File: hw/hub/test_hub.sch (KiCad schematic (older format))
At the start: 104 parts, among them J1 ARM-SWD, P1 USB_OTG, P2 5V_SEL, P3 5V_EXT, P4 USB1, P5 USB2, P6 USB3, P7 UART, SW1 RST, SW2 BOOT, U1 USB2514B, U2 MIC550X, U3 stm32f072x, U4 AP2171, U5 AP2171, U6 AP2171, U7 LT6106, U8 LT6106, U9 LT6106, Y1 24MHz

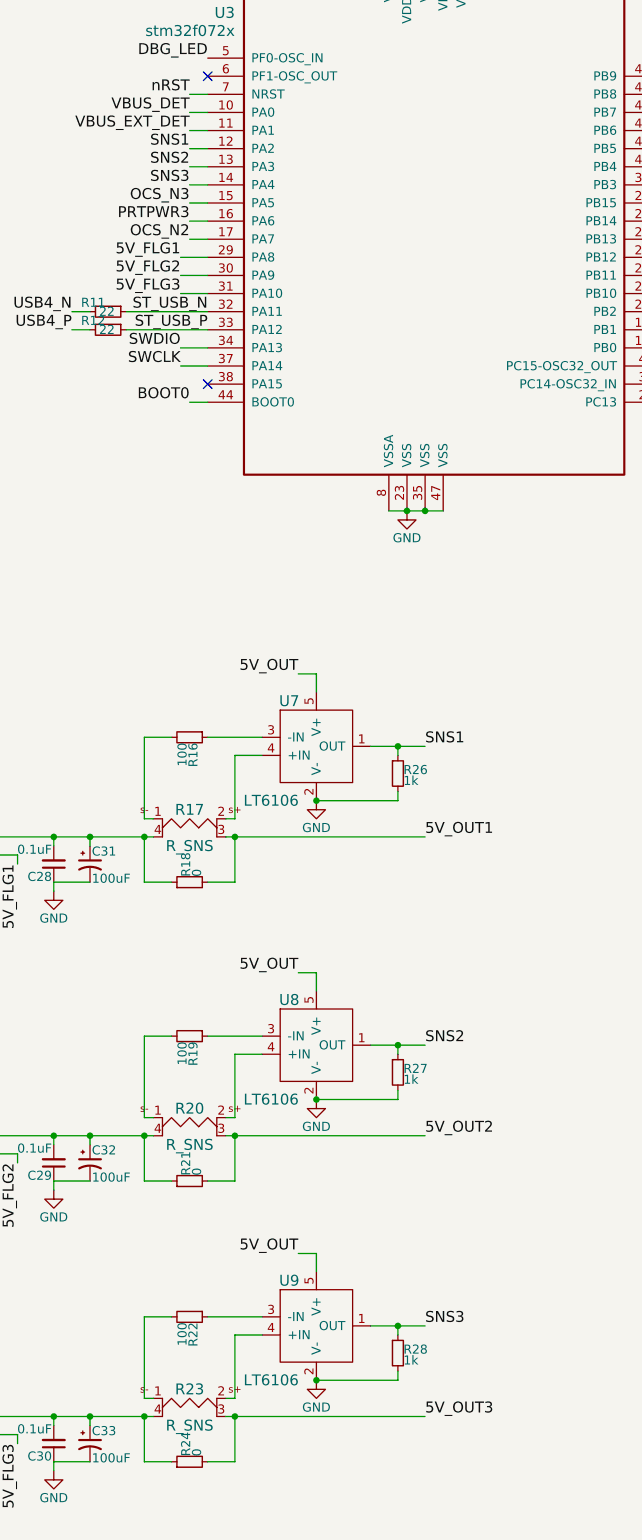
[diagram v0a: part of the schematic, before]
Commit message: Begin removing sense resistors from hub
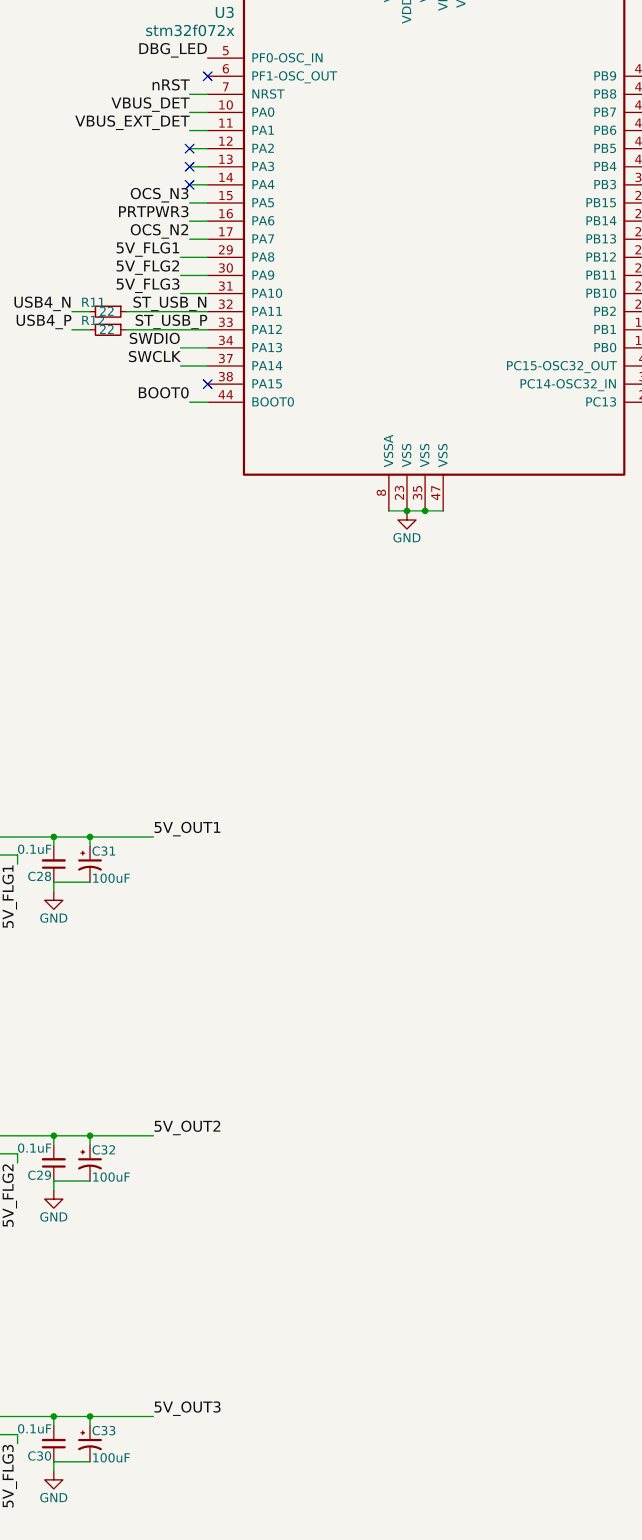
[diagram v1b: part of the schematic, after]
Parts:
- removed R16, R19, R22: 100, Resistors_SMD:R_0603, symbol R_Small
- removed R17, R20, R23: R_SNS, footprints:LVK12, symbol R_SNS
- removed R18, R21, R24: 0, Resistors_SMD:R_0603, symbol R_Small
- removed R26, R27, R28: 1k, Resistors_SMD:R_0603, symbol R_Small
- removed U7, U8, U9: LT6106, footprints:TSOT-23-5, symbol LT6106-RESCUE-test_hub
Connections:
- net 5V_OUT1: now also C28.2, C31.1, U4.1 (OUT)
- net 5V_OUT2: now also C29.2, C32.1, U5.1 (OUT)
- net 5V_OUT3: now also C30.2, C33.1, U6.1 (OUT)
- net SNS1: no longer names the net of U3.12 (PA2)
- net SNS2: no longer names the net of U3.13 (PA3)
- net SNS3: no longer names the net of U3.14 (PA4)
- no-connect marks 13 -> 16

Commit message: Update test_hub
No more rescued components
Ripped up all traces
Starting layout again
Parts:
- removed D1: 3V, LEDs:LED_0603, symbol LED-RESCUE-test_hub
- removed D2: DBG, LEDs:LED_0603, symbol LED-RESCUE-test_hub
- removed D3: 5V_EN3, LEDs:LED_0603, symbol LED-RESCUE-test_hub
- removed D4: 5V_EN2, LEDs:LED_0603, symbol LED-RESCUE-test_hub
- removed D5: 5V_EN1, LEDs:LED_0603, symbol LED-RESCUE-test_hub
- removed D6: LED2, LEDs:LED_0603, symbol LED-RESCUE-test_hub
- removed D7: LED1, LEDs:LED_0603, symbol LED-RESCUE-test_hub
- removed D8: LED0, LEDs:LED_0603, symbol LED-RESCUE-test_hub
- removed P1: USB_OTG, footprints:10118193-0001LF, symbol USB_OTG-RESCUE-test_hub
- removed P4: USB1, footprints:292303-1, symbol USB_A-RESCUE-test_hub
- removed P5: USB2, footprints:292303-1, symbol USB_A-RESCUE-test_hub
- removed P6: USB3, footprints:292303-1, symbol USB_A-RESCUE-test_hub
- added C35: 0.1uF, Capacitors_SMD:C_0603, symbol C_Small
- added D1: 3V, LEDs:LED_0805, symbol LED
- added D2: DBG, LEDs:LED_0805, symbol LED
- added D3: 5V_EN3, LEDs:LED_0805, symbol LED
- added D4: 5V_EN2, LEDs:LED_0805, symbol LED
- added D5: 5V_EN1, LEDs:LED_0805, symbol LED
- added D6: LED3, LEDs:LED_0805, symbol LED
- added D7: LED2, LEDs:LED_0805, symbol LED
- added D8: LED1, LEDs:LED_0805, symbol LED
- added FB10, FB7, FB8, FB9: Ferrite_Bead, Resistors_SMD:R_0603, symbol Ferrite_Bead-RESCUE-test_hub
- added J2, J3: USB_OTG, footprints:USB_MICRO_B, symbol USB_OTG
- added J4, J5, J6: USB_A, footprints:292303-1, symbol USB_A
- added R16: 330, Resistors_SMD:R_0603, symbol R_Small
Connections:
- net LED0 is gone; now on net LED1: R36.2, U3.2 (PC13)
- net +5V: now also FB3.2, FB5.1
- net 5V_OUT2: now also FB8.1; no longer FB4.1
- net 5V_OUT3: now also FB10.1; no longer FB6.1
- net GND: now also FB4.2, FB6.1, C35.1, D1.1 (K), D2.1 (K), D3.1 (K), D4.1 (K), D5.1 (K), D6.1 (K), D7.1 (K), D8.1 (K), FB7.1, FB9.1, R16.2; no longer FB3.1, FB5.1
- net GNDPWR: now also C35.2, J2.6 (Shield), J3.6 (Shield), J4.5 (Shield), J5.5 (Shield), J6.5 (Shield), R16.1
- net LED1: no longer R35.2, U3.3 (PC14-OSC32_IN)
- net LED2: now also R35.2, U3.3 (PC14-OSC32_IN); no longer R34.2, U3.4 (PC15-OSC32_OUT)
- net USB1_N: now also J4.2 (D-)
- net USB1_P: now also J4.3 (D+)
- net USB2_N: now also J5.2 (D-)
- net USB2_P: now also J5.3 (D+)
- net USB3_N: now also J6.2 (D-)
- net USB3_P: now also J6.3 (D+)
- net USB_UP_N: now also J2.2 (D-)
- net USB_UP_P: now also J2.3 (D+)
- net at FB6.2: now also J3.5 (GND)
- net at FB5.2: now also J3.1 (VBUS)
- net at R30.1: now also D2.2 (A)
- net at R31.1: now also D3.2 (A)
- net at R32.1: now also D4.2 (A)
- net at R33.1: now also D5.2 (A)
- net at R34.1: now also D6.2 (A)
- net at R35.1: now also D7.2 (A)
- net at R36.1: now also D8.2 (A)
- net at FB1.2: now also J4.4 (GND)
- net at FB2.2: now also J4.1 (VBUS)
- net at R29.1: now also D1.2 (A)
- new net: FB3.1, J2.1 (VBUS)
- new net: FB4.1, J2.5 (GND)
- new net: FB7.2, J5.4 (GND)
- new net: FB8.2, J5.1 (VBUS)
- new net: FB9.2, J6.4 (GND)
- new net: FB10.2, J6.1 (VBUS)
- new net LED3: R34.2, U3.4 (PC15-OSC32_OUT)
- no-connect marks 16 -> 19
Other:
- moved on the sheet: C14, C15, FB1, FB2, P2, P3, R10, R7, R8, R9

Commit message: More test_hub work
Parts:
- added C36, C37: 1uF, Capacitors_SMD:C_0603, symbol C_Small
- FB1, FB10, FB2, FB3, FB4, FB5, FB6, FB7, FB8, FB9: MPN BLM18EG221SN1D -> CIS10P221NC
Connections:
- net GND: now also C36.1, C37.1
- net at C3.2, U1.14 (CRFILT): now also C37.2
- net at C4.2, U1.34 (PLLFILT): now also C36.2
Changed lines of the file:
@@
 F 2 "Resistors_SMD:R_0603" H 14450 3250 60  0001 C CNN
 F 3 "" H 14450 3250 60  0000 C CNN
-F 4 "BLM18EG221SN1D" H 14450 3200 60  0001 C CNN "MPN"
+F 4 "CIS10P221NC" H 14450 3200 60  0001 C CNN "MPN"
 	1    14450 3200
 	1    0    0    -1
@@
 F 2 "Resistors_SMD:R_0603" H 14450 3900 60  0001 C CNN
 F 3 "" H 14450 3900 60  0000 C CNN
-F 4 "BLM18EG221SN1D" H 14450 3850 60  0001 C CNN "MPN"
+F 4 "CIS10P221NC" H 14450 3850 60  0001 C CNN "MPN"
 	1    14450 3850
 	1    0    0    -1
@@
 F 2 "Resistors_SMD:R_0603" H 2450 7200 60  0001 C CNN
 F 3 "" H 2450 7200 60  0000 C CNN
-F 4 "BLM18EG221SN1D" H 2450 7150 60  0001 C CNN "MPN"
+F 4 "CIS10P221NC" H 2450 7150 60  0001 C CNN "MPN"
 	1    2450 7150
 	1    0    0    -1
@@
 F 2 "Resistors_SMD:R_0603" H 2450 7850 60  0001 C CNN
 F 3 "" H 2450 7850 60  0000 C CNN
-F 4 "BLM18EG221SN1D" H 2450 7800 60  0001 C CNN "MPN"
+F 4 "CIS10P221NC" H 2450 7800 60  0001 C CNN "MPN"
 	1    2450 7800
 	1    0    0    -1
@@
 	2050 4100 2050 4150
 Wire Wire Line
-	2850 4100 2050 4100
+	1800 4100 2850 4100
 Connection ~ 2450 5800
 Wire Wire Line
 	2450 5800 2450 5850
 Wire Wire Line
-	2700 5800 2450 5800
+	2200 5800 2700 5800
 Wire Wire Line
 	2850 5600 2700 5600
@@
 	2450 5500 2450 5600
 Wire Wire Line
-	2450 5500 2850 5500
+	2200 5500 2850 5500
 Wire Wire Line
 	2850 4800 2650 4800
@@
 F 2 "Resistors_SMD:R_0603" H 2450 8600 60  0001 C CNN
 F 3 "" H 2450 8600 60  0000 C CNN
-F 4 "BLM18EG221SN1D" H 2450 8550 60  0001 C CNN "MPN"
+F 4 "CIS10P221NC" H 2450 8550 60  0001 C CNN "MPN"
 	1    2450 8550
 	-1   0    0    1
@@
 F 2 "Resistors_SMD:R_0603" H 2450 9250 60  0001 C CNN
 F 3 "" H 2450 9250 60  0000 C CNN
-F 4 "BLM18EG221SN1D" H 2450 9200 60  0001 C CNN "MPN"
+F 4 "CIS10P221NC" H 2450 9200 60  0001 C CNN "MPN"
 	1    2450 9200
 	-1   0    0    1
@@
 F 2 "Resistors_SMD:R_0603" H 14450 4450 60  0001 C CNN
 F 3 "" H 14450 4450 60  0000 C CNN
-F 4 "BLM18EG221SN1D" H 14450 4400 60  0001 C CNN "MPN"
+F 4 "CIS10P221NC" H 14450 4400 60  0001 C CNN "MPN"
 	1    14450 4400
 	1    0    0    -1
@@
 F 2 "Resistors_SMD:R_0603" H 14450 5100 60  0001 C CNN
 F 3 "" H 14450 5100 60  0000 C CNN
-F 4 "BLM18EG221SN1D" H 14450 5050 60  0001 C CNN "MPN"
+F 4 "CIS10P221NC" H 14450 5050 60  0001 C CNN "MPN"
 	1    14450 5050
 	1    0    0    -1
@@
 F 2 "Resistors_SMD:R_0603" H 14450 5650 60  0001 C CNN
 F 3 "" H 14450 5650 60  0000 C CNN
-F 4 "BLM18EG221SN1D" H 14450 5600 60  0001 C CNN "MPN"
+F 4 "CIS10P221NC" H 14450 5600 60  0001 C CNN "MPN"
 	1    14450 5600
 	1    0    0    -1
@@
 F 2 "Resistors_SMD:R_0603" H 14450 6300 60  0001 C CNN
 F 3 "" H 14450 6300 60  0000 C CNN
-F 4 "BLM18EG221SN1D" H 14450 6250 60  0001 C CNN "MPN"
+F 4 "CIS10P221NC" H 14450 6250 60  0001 C CNN "MPN"
 	1    14450 6250
 	1    0    0    -1
@@
 	1400 7800 1250 7800
 Connection ~ 1400 7800
+$Comp
+L C_Small C36
+U 1 1 5917EE32
+P 2200 5700
+F 0 "C36" H 2210 5770 50  0000 L CNN
+F 1 "1uF" H 2210 5620 50  0000 L CNN
+F 2 "Capacitors_SMD:C_0603" H 2200 5700 50  0001 C CNN
+F 3 "" H 2200 5700 50  0000 C CNN
+F 4 "GRM188R61C105KA93D" H 2200 5700 60  0001 C CNN "MPN"
+	1    2200 5700
+	-1   0    0    1
+$EndComp
+Wire Wire Line
+	2200 5600 2200 5500
+Connection ~ 2450 5500
+$Comp
+L C_Small C37
+U 1 1 59182393
+P 1800 4250
+F 0 "C37" H 1810 4320 50  0000 L CNN
+F 1 "1uF" H 1810 4170 50  0000 L CNN
+F 2 "Capacitors_SMD:C_0603" H 1800 4250 50  0001 C CNN
+F 3 "" H 1800 4250 50  0000 C CNN
+F 4 "GRM188R61C105KA93D" H 1800 4250 60  0001 C CNN "MPN"
+	1    1800 4250
+	-1   0    0    1
+$EndComp
+Wire Wire Line
+	1800 4150 1800 4100
+Connection ~ 2050 4100
+Wire Wire Line
+	1800 4350 1800 4400
+Wire Wire Line
+	1800 4400 2050 4400
 $EndSCHEMATC

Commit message: Continued routing work on test_hub
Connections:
- net +5V: no longer FB5.1
- net 5V_EXT: now also FB5.2
- net at J3.1 (VBUS): now also FB5.1; no longer FB5.2
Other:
- moved on the sheet: FB5
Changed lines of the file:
@@
 	2600 7800 2650 7800
 Wire Wire Line
-	1400 7850 1400 7750
+	1400 7750 1400 7850
 Wire Wire Line
 	1500 7750 1500 7800
@@
 	0    -1   -1   0
 $EndComp
-$Comp
-L +5V #PWR056
-U 1 1 5917EA63
-P 2650 8550
-F 0 "#PWR056" H 2650 8400 50  0001 C CNN
-F 1 "+5V" H 2650 8690 50  0000 C CNN
-F 2 "" H 2650 8550 50  0000 C CNN
-F 3 "" H 2650 8550 50  0000 C CNN
-	1    2650 8550
-	0    1    1    0
-$EndComp
 NoConn ~ 1800 8950
 $Comp
-L GNDPWR #PWR057
+L GNDPWR #PWR056
 U 1 1 5917EA6A
 P 1400 9250
-F 0 "#PWR057" H 1400 9050 50  0001 C CNN
+F 0 "#PWR056" H 1400 9050 50  0001 C CNN
 F 1 "GNDPWR" H 1400 9120 50  0000 C CNN
 F 2 "" H 1400 9200 50  0000 C CNN
@@
 F 4 "CIS10P221NC" H 2450 8550 60  0001 C CNN "MPN"
 	1    2450 8550
-	-1   0    0    1
+	1    0    0    -1
 $EndComp
 $Comp
@@
 	15150 3200 14600 3200
 $Comp
-L GND #PWR058
+L GND #PWR057
 U 1 1 591825FD
 P 14250 4400
-F 0 "#PWR058" H 14250 4150 50  0001 C CNN
+F 0 "#PWR057" H 14250 4150 50  0001 C CNN
 F 1 "GND" H 14250 4250 50  0000 C CNN
 F 2 "" H 14250 4400 50  0000 C CNN
@@
 $EndComp
 $Comp
-L GNDPWR #PWR059
+L GNDPWR #PWR058
 U 1 1 59182611
 P 15500 4450
-F 0 "#PWR059" H 15500 4250 50  0001 C CNN
+F 0 "#PWR058" H 15500 4250 50  0001 C CNN
 F 1 "GNDPWR" H 15500 4320 50  0000 C CNN
 F 2 "" H 15500 4400 50  0000 C CNN
@@
 	15150 4400 14600 4400
 $Comp
-L GND #PWR060
+L GND #PWR059
 U 1 1 591827F0
 P 14250 5600
-F 0 "#PWR060" H 14250 5350 50  0001 C CNN
+F 0 "#PWR059" H 14250 5350 50  0001 C CNN
 F 1 "GND" H 14250 5450 50  0000 C CNN
 F 2 "" H 14250 5600 50  0000 C CNN
@@
 $EndComp
 $Comp
-L GNDPWR #PWR061
+L GNDPWR #PWR060
 U 1 1 59182804
 P 15500 5650
-F 0 "#PWR061" H 15500 5450 50  0001 C CNN
+F 0 "#PWR060" H 15500 5450 50  0001 C CNN
 F 1 "GNDPWR" H 15500 5520 50  0000 C CNN
 F 2 "" H 15500 5600 50  0000 C CNN
@@
 $EndComp
 $Comp
-L PWR_FLAG #FLG062
+L PWR_FLAG #FLG061
 U 1 1 59174339
 P 1850 7800
-F 0 "#FLG062" H 1850 7895 50  0001 C CNN
+F 0 "#FLG061" H 1850 7895 50  0001 C CNN
 F 1 "PWR_FLAG" H 1850 7980 50  0000 C CNN
 F 2 "" H 1850 7800 50  0000 C CNN
@@
 $EndComp
 $Comp
-L PWR_FLAG #FLG063
+L PWR_FLAG #FLG062
 U 1 1 59174704
 P 1850 7150
-F 0 "#FLG063" H 1850 7245 50  0001 C CNN
+F 0 "#FLG062" H 1850 7245 50  0001 C CNN
 F 1 "PWR_FLAG" H 1850 7330 50  0000 C CNN
 F 2 "" H 1850 7150 50  0000 C CNN
@@
 Connection ~ 1850 7800
 $Comp
-L GND #PWR064
+L GND #PWR063
 U 1 1 58A5C239
 P 1200 1150
-F 0 "#PWR064" H 1200 900 50  0001 C CNN
+F 0 "#PWR063" H 1200 900 50  0001 C CNN
 F 1 "GND" H 1200 1000 50  0000 C CNN
 F 2 "" H 1200 1150 50  0000 C CNN
@@
 	1200 1100 1200 1150
 $Comp
-L PWR_FLAG #FLG065
+L PWR_FLAG #FLG064
 U 1 1 59178058
 P 1250 7800
-F 0 "#FLG065" H 1250 7895 50  0001 C CNN
+F 0 "#FLG064" H 1250 7895 50  0001 C CNN
 F 1 "PWR_FLAG" H 1250 7980 50  0000 C CNN
 F 2 "" H 1250 7800 50  0000 C CNN
@@
 Wire Wire Line
 	1800 4400 2050 4400
+Text Label 2650 8550 0    60   ~ 0
+5V_EXT
+Connection ~ 2050 8550
+$Comp
+L PWR_FLAG #FLG065
+U 1 1 591F43BC
+P 2050 8550
+F 0 "#FLG065" H 2050 8645 50  0001 C CNN
+F 1 "PWR_FLAG" H 2050 8730 50  0000 C CNN
+F 2 "" H 2050 8550 50  0000 C CNN
+F 3 "" H 2050 8550 50  0000 C CNN
+	1    2050 8550
+	1    0    0    -1
+$EndComp
 $EndSCHEMATC

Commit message: Almost done with test_hub layout
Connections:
- net 5V_EN2: now also U3.27 (PB14); no longer U3.26 (PB13)
- net 5V_EN3: now also U3.29 (PA8); no longer U3.27 (PB14)
- net 5V_FLG1: now also U3.26 (PB13); no longer U3.29 (PA8)
- net 5V_FLG2: now also U3.28 (PB15); no longer U3.30 (PA9)
- net 5V_FLG3: now also U3.30 (PA9); no longer U3.31 (PA10)
- net CFG_SEL1: now also U3.14 (PA4); no longer U3.40 (PB4)
- net HUB_RST_N: now also U3.13 (PA3); no longer U3.28 (PB15)
- net SUSP_IND: now also U3.11 (PA1); no longer U3.39 (PB3)
- net VBUS_DET: now also U3.12 (PA2); no longer U3.10 (PA0)
- net VBUS_EXT_DET: now also U3.10 (PA0); no longer U3.11 (PA1)
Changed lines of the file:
@@
 Text Label 1700 2750 0    60   ~ 0
 CFG_SEL1
-Text Label 11750 3550 0    60   ~ 0
+Text Label 9000 3350 2    60   ~ 0
 HUB_RST_N
-Text Label 9000 3050 2    60   ~ 0
+Text Label 9000 3250 2    60   ~ 0
 VBUS_DET
-Text Label 11750 3350 0    60   ~ 0
+Text Label 9000 3450 2    60   ~ 0
 CFG_SEL1
 Text Label 2650 5000 2    60   ~ 0
 SUSP_IND
-Text Label 11750 3450 0    60   ~ 0
+Text Label 9000 3150 2    60   ~ 0
 SUSP_IND
 Text Label 11750 4150 0    60   ~ 0
@@
 Text Label 11750 3850 0    60   ~ 0
 5V_EN1
-Text Label 11750 3750 0    60   ~ 0
+Text Label 11750 3650 0    60   ~ 0
 5V_EN2
-Text Label 11750 3650 0    60   ~ 0
+Text Label 8950 3850 2    60   ~ 0
 5V_EN3
 $Comp
@@
 Text Label 3400 8500 2    60   ~ 0
 5V_OUT
-Text Label 9000 3150 2    60   ~ 0
+Text Label 9000 3050 2    60   ~ 0
 VBUS_EXT_DET
 $Comp
@@
 	1    0    0    -1
 $EndComp
-Text Label 8950 3850 2    60   ~ 0
+Text Label 11750 3750 0    60   ~ 0
 5V_FLG1
+Text Label 11750 3550 0    60   ~ 0
+5V_FLG2
 Text Label 8950 3950 2    60   ~ 0
-5V_FLG2
-Text Label 8950 4050 2    60   ~ 0
 5V_FLG3
 $Comp
@@
 Text Label 9100 4250 2    60   ~ 0
 ST_USB_P
-NoConn ~ 9000 3250
-NoConn ~ 9000 3350
-NoConn ~ 9000 3450
+NoConn ~ 11750 3350
+NoConn ~ 11750 3450
+NoConn ~ 8950 4050
 $Comp
 L Ferrite_Bead-RESCUE-test_hub FB3
